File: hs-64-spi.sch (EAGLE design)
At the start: 25 parts, among them J1 DF40C-70DP-0.4V(51), J2 A79622-001, U1 RHD2064_BGA, U2 ADXL335_IDAX

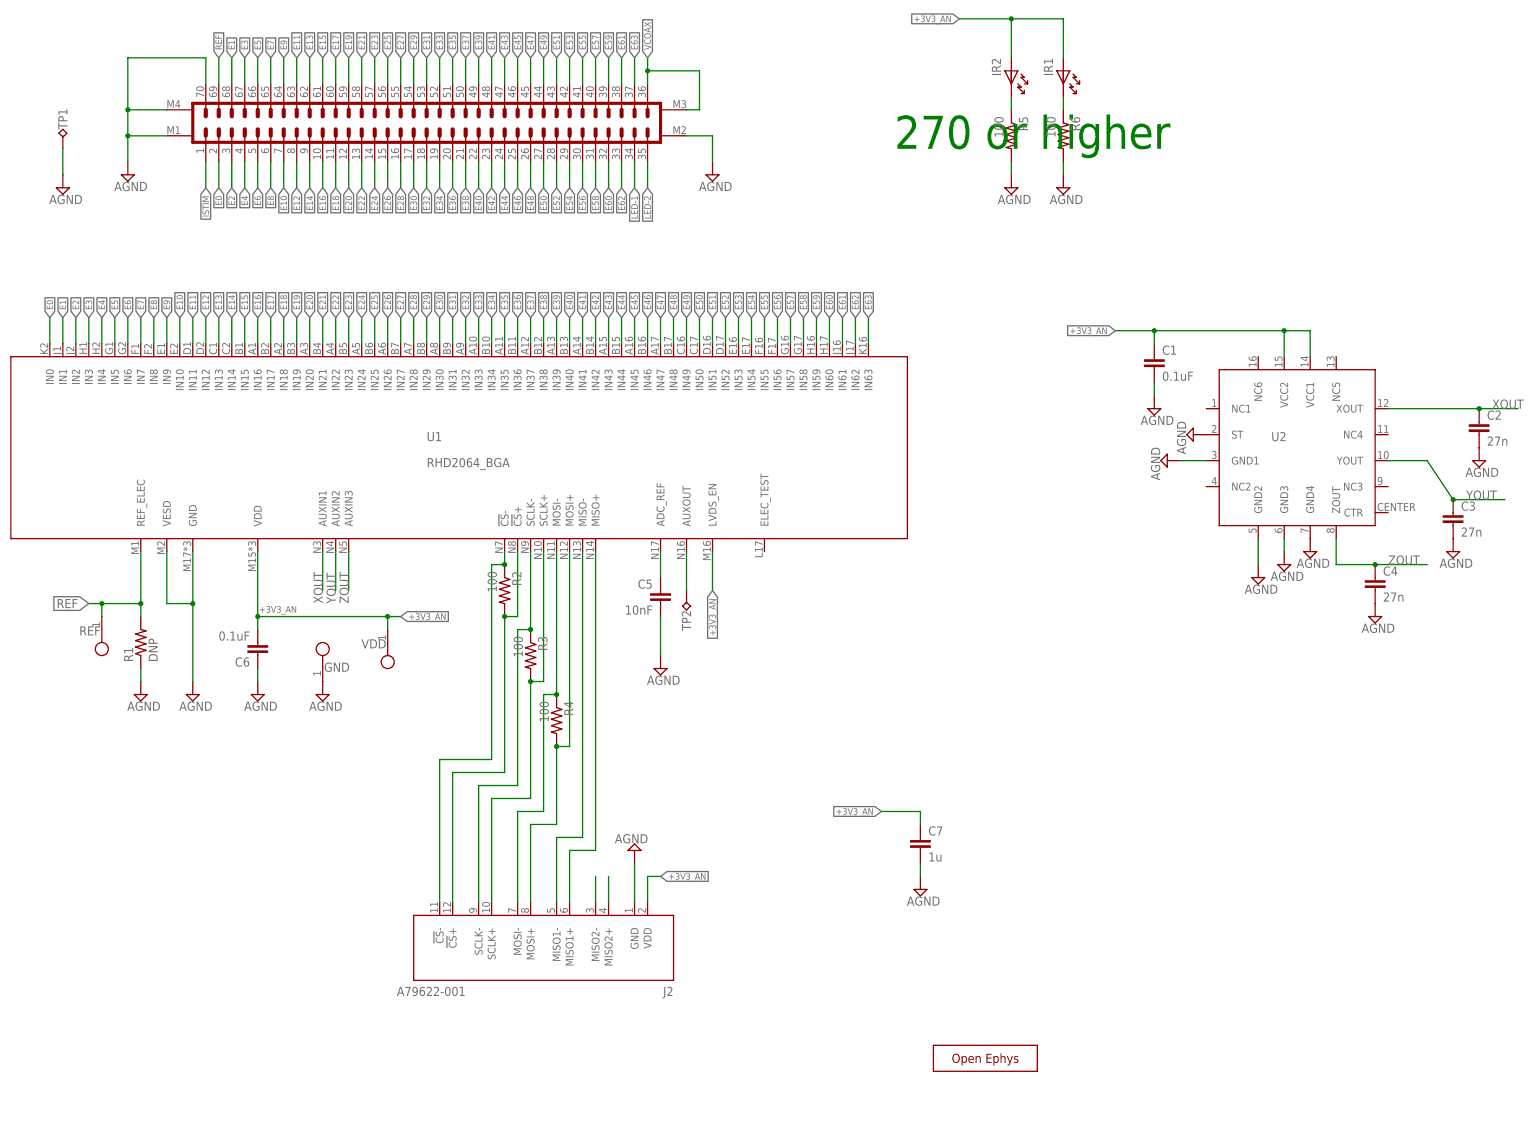
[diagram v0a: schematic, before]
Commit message: Added PCB design files for the new version 1.1.
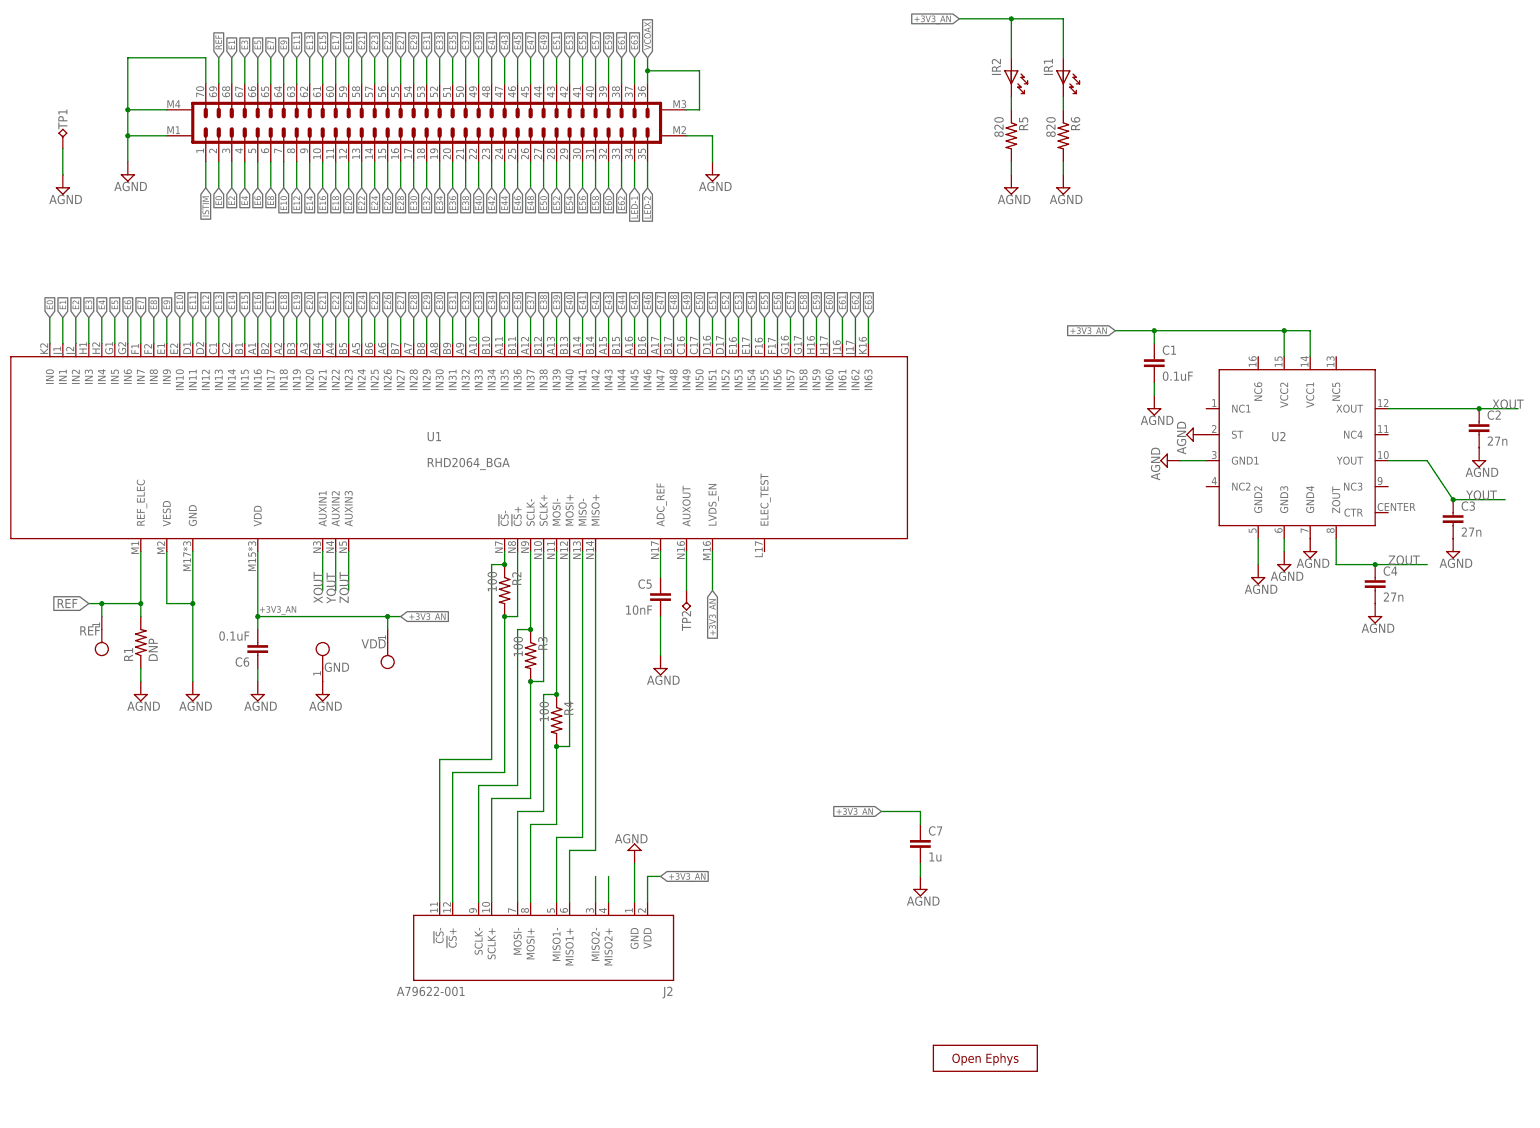
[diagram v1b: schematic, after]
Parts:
- R5, R6: value 100 -> 820
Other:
- note removed: "270 or higher"

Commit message: Corrected C7 value to 4.7uF.
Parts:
- C7: value 1u -> 4.7u
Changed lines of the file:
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@@
 <part name="R1" library="jonnew" deviceset="R" device="_0603" value="DNP"/>
 <part name="SUPPLY11" library="jonnew" deviceset="AGND" device=""/>
-<part name="C7" library="jonnew" deviceset="C" device="_0402" value="1u"/>
+<part name="C7" library="jonnew" deviceset="C" device="_0402" value="4.7u"/>
 <part name="FRAME1" library="frames" deviceset="A3L-LOC" device=""/>
 <part name="GND" library="RHD2000_eval_board" deviceset="TESTPOINT" device="_SMALL"/>

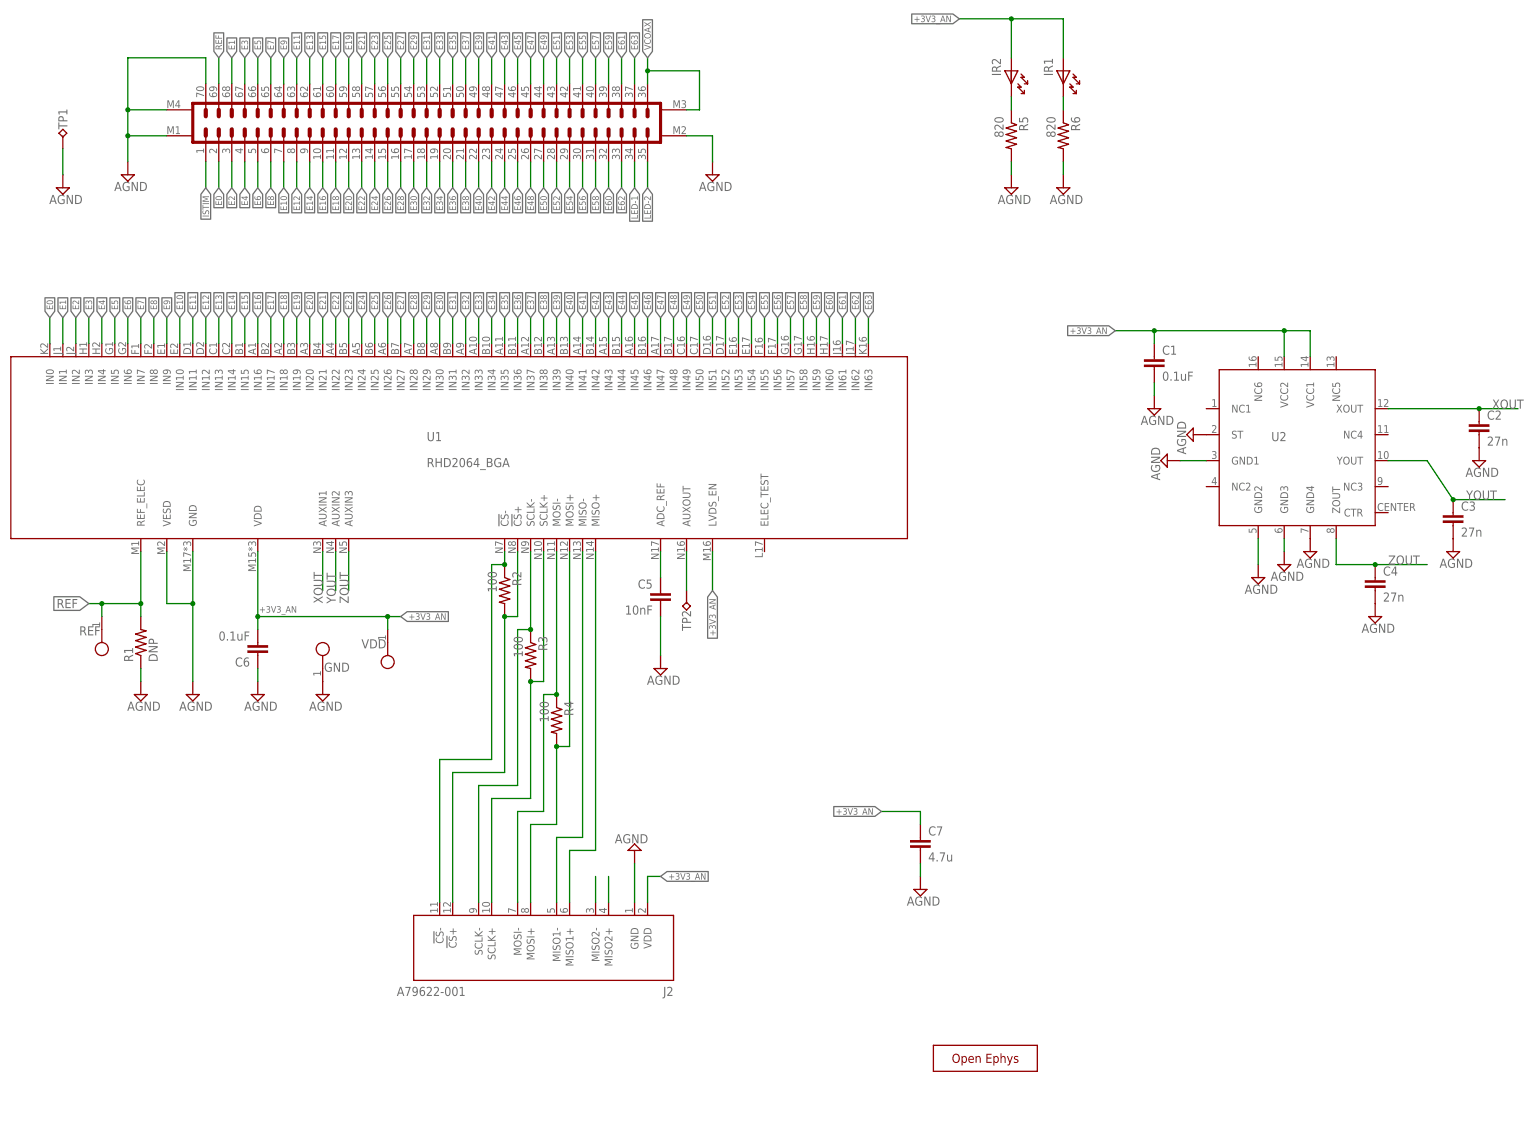
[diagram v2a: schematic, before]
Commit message: Updated Hirose (J1) schematic.
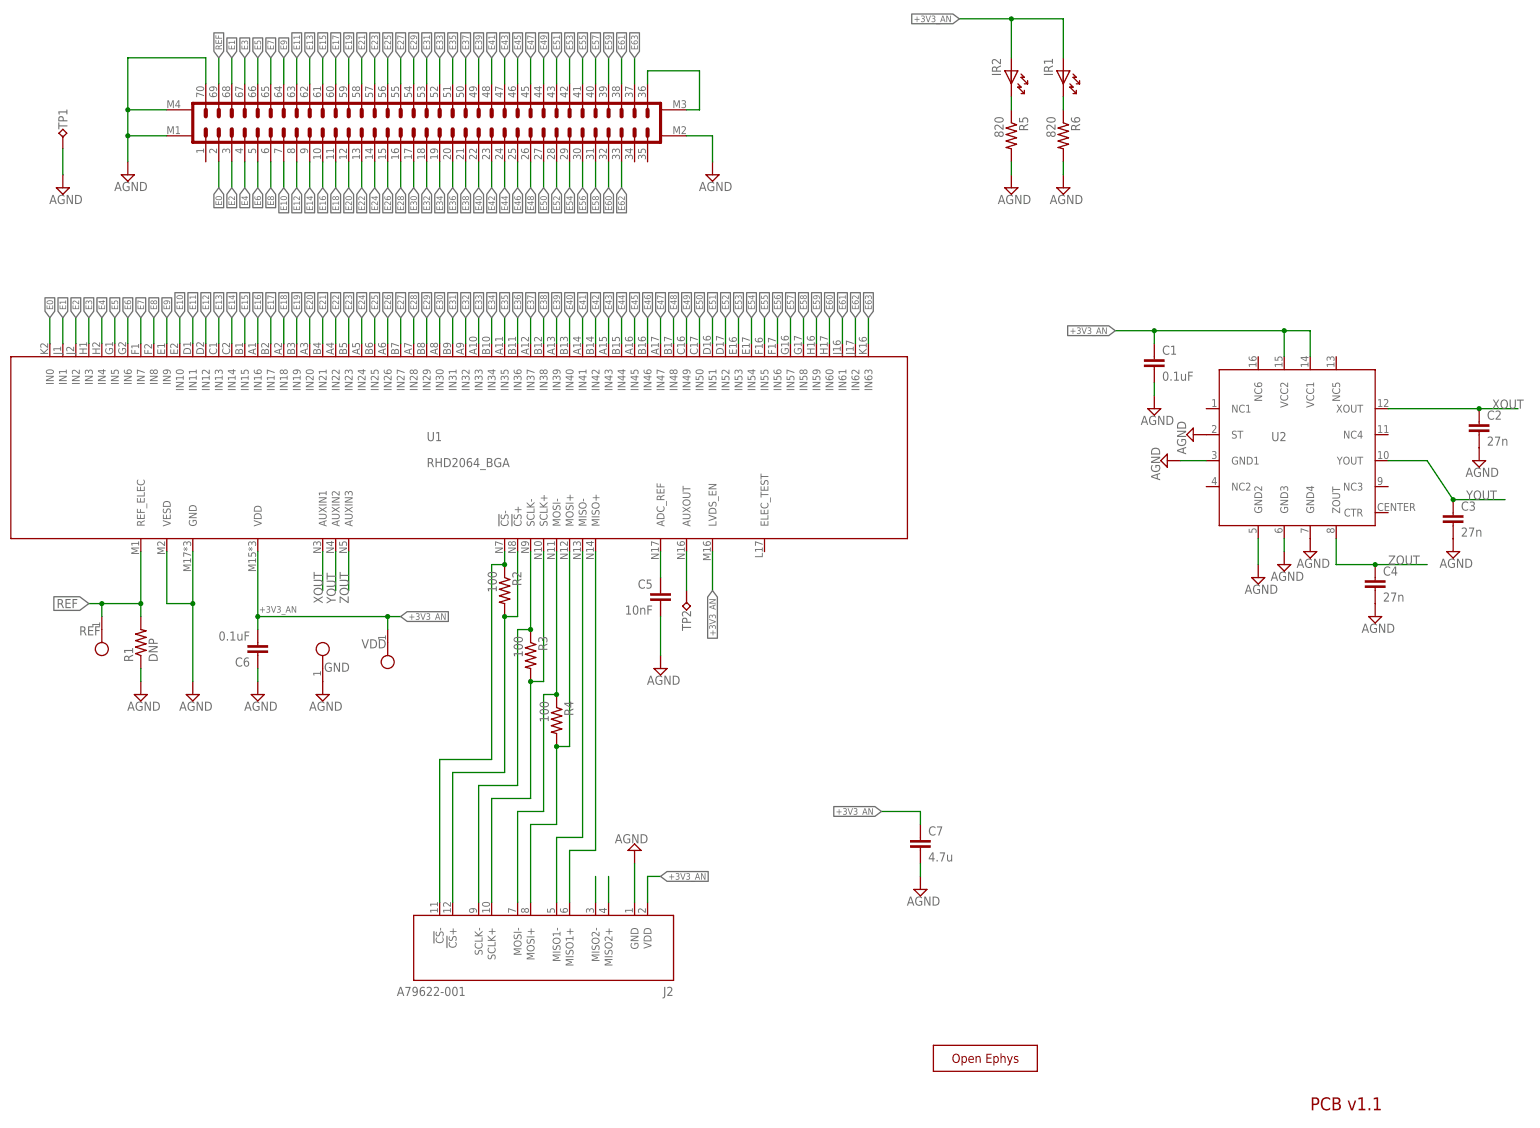
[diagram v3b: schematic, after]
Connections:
- removed net ISTIM: J1.1
- removed net LED-1: J1.34
- removed net LED-2: J1.35
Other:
- note added: "PCB v1.1"
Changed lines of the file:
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@@
 <sheet>
 <plain>
+<text x="307.34" y="12.7" size="2.54" layer="94">PCB v1.1</text>
 </plain>
 <instances>
@@
 </busses>
 <nets>
-<net name="LED-2" class="0">
-<segment>
-<pinref part="J1" gate="G$1" pin="35"/>
-<wire x1="177.8" y1="198.12" x2="177.8" y2="193.04" width="0.1524" layer="91"/>
-<label x="177.8" y="193.04" size="1.27" layer="95" rot="R270" xref="yes"/>
-</segment>
-</net>
 <net name="VCOAX" class="0">
 <segment>
 <pinref part="J1" gate="G$1" pin="36"/>
 <wire x1="177.8" y1="213.36" x2="177.8" y2="215.9" width="0.1524" layer="91"/>
-<label x="177.8" y="218.44" size="1.27" layer="95" rot="R90" xref="yes"/>
-<wire x1="177.8" y1="215.9" x2="177.8" y2="218.44" width="0.1524" layer="91"/>
 <wire x1="177.8" y1="215.9" x2="187.96" y2="215.9" width="0.1524" layer="91"/>
 <wire x1="187.96" y1="215.9" x2="187.96" y2="208.28" width="0.1524" layer="91"/>
-<junction x="177.8" y="215.9"/>
 <pinref part="J1" gate="G$1" pin="M3"/>
 <wire x1="187.96" y1="208.28" x2="185.42" y2="208.28" width="0.1524" layer="91"/>
@@
 <label x="134.62" y="193.04" size="1.27" layer="95" rot="MR270" xref="yes"/>
 <pinref part="J1" gate="G$1" pin="18"/>
-</segment>
-</net>
-<net name="LED-1" class="0">
-<segment>
-<pinref part="J1" gate="G$1" pin="34"/>
-<wire x1="175.26" y1="193.04" x2="175.26" y2="198.12" width="0.1524" layer="91"/>
-<label x="175.26" y="193.04" size="1.27" layer="95" rot="R270" xref="yes"/>
 </segment>
 </net>
@@
 </segment>
 </net>
-<net name="ISTIM" class="0">
-<segment>
-<pinref part="J1" gate="G$1" pin="1"/>
-<wire x1="91.44" y1="198.12" x2="91.44" y2="193.04" width="0.1524" layer="91"/>
-<label x="91.44" y="193.04" size="1.27" layer="95" rot="R270" xref="yes"/>
-</segment>
-</net>
